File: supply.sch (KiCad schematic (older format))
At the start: 93 parts, among them IC12 74HC00PW, IC13 SN74LVC1G126DCKR, IC4 TPS7A0518PDBVT, J12 533980471, T3 BSS138APW, U1 LM3671MF-3.3/NOPB, U2 LM62440-Q1, U3 SN74LXC1T45DBVR, U5 LM3671MF-3.3/NOPB, U6 SIC477ED-T1-GE3

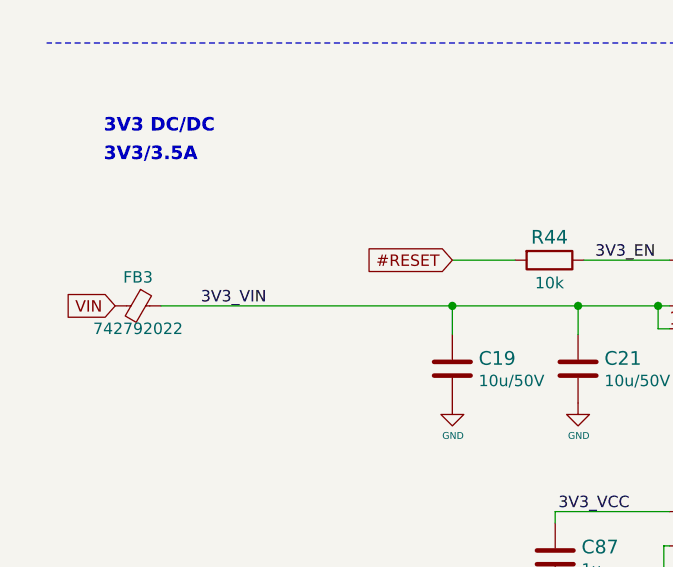
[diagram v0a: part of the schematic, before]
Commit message: Update MPS for FB2 FB3
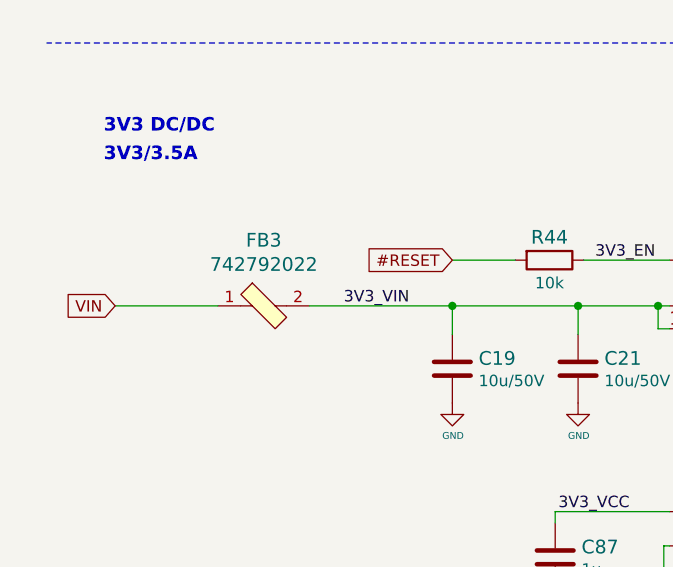
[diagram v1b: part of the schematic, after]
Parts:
- removed FB3: 742792022, jetson-nano-baseboard-footprints:0805-cap, symbol jetson-nano-baseboard:Ferrite_Bead_Small
- added FB3: 742792022, antmicro-footprints:0805-res, symbol antmicroFerriteBeadsandChips:742792022
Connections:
- net 3V3_VIN: now also FB3.2
- net VIN: now also FB3.1
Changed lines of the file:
@@
 Text Label 3050 5175 0    50   ~ 0
 3V3_EN
-$Comp
-L jetson-nano-baseboard:Ferrite_Bead_Small FB3
-U 1 1 61E2F9C4
-P 1050 5375
-F 0 "FB3" V 925 5375 50  0000 C CNN
-F 1 "742792022 " V 1150 5375 50  0000 C CNN
-F 2 "jetson-nano-baseboard-footprints:0805-cap" V 980 5375 50  0001 C CNN
-F 3 "~" H 1050 5375 50  0001 C CNN
-	1    1050 5375
-	0    1    1    0
-$EndComp
 Text GLabel 950  5375 0    50   Input ~ 0
 VIN
@@
 Text Label 3200 6275 2    50   ~ 0
 3V3_VCC
-Text Label 1325 5375 0    50   ~ 0
+Text Label 1950 5375 0    50   ~ 0
 3V3_VIN
 Text Label 4675 5750 0    50   ~ 0
@@
 	5775 4675 6225 4675
 Wire Wire Line
-	1150 5375 2425 5375
+	1800 5375 2425 5375
 Text Notes 15575 5400 0    59   ~ 12
 FAN 5V
@@
 Text GLabel 12350 6625 0    50   Input ~ 0
 1V8_SYS
+$Comp
+L antmicroFerriteBeadsandChips:742792022 FB3
+U 1 1 620C3704
+P 1600 5375
+F 0 "FB3" H 1600 5662 60  0000 C CNN
+F 1 "742792022" H 1600 5556 60  0000 C CNN
+F 2 "antmicro-footprints:0805-res" H 1800 5575 60  0001 L CNN
+F 3 "https://www.we-online.com/katalog/datasheet/742792022.pdf" H 1800 5675 60  0001 L CNN
+F 4 "742792022" H 1800 5875 60  0001 L CNN "MPN"
+F 5 "Wurth Electronic" H 1800 6475 60  0001 L CNN "Manufacturer"
+	1    1600 5375
+	1    0    0    -1
+$EndComp
+Wire Wire Line
+	1400 5375 950  5375
 $EndSCHEMATC

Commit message: Update libraries
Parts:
- FB3: footprint antmicro-footprints:0805-res -> jetson-nano-baseboard-footprints:0805-res; symbol antmicroFerriteBeadsandChips:742792022 -> jetson-nano-baseboard:742792022
- R76, R93: footprint antmicro-footprints:0402-res -> jetson-nano-baseboard-footprints:0402-res; symbol antmicroResistors0402:R_0R_0402 -> jetson-nano-baseboard:R_0R_0402
- U6: footprint antmicro-footprints:SIC47XED-T1-GE3 -> jetson-nano-baseboard-footprints:SIC47XED-T1-GE3; symbol antmicroDCDCConverters:SIC477ED-T1-GE3 -> jetson-nano-baseboard:SIC477ED-T1-GE3
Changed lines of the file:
@@
 	5625 1125 5700 1125
 $Comp
-L antmicroResistors0402:R_0R_0402 R93
+L jetson-nano-baseboard:R_0R_0402 R93
 U 1 1 625DF619
 P 5825 3050
 F 0 "R93" H 5825 3173 60  0000 C CNN
 F 1 "R_0R_0402" H 5825 2900 60  0001 C CNN
-F 2 "antmicro-footprints:0402-res" H 6025 3250 60  0001 L CNN
+F 2 "jetson-nano-baseboard-footprints:0402-res" H 6025 3250 60  0001 L CNN
 F 3 "" H 5825 3050 50  0001 C CNN
 F 4 "PANASONIC" H 6025 3450 60  0001 L CNN "Manufacturer"
@@
 VDD_5V_DCDC
 $Comp
-L antmicroResistors0402:R_0R_0402 R76
+L jetson-nano-baseboard:R_0R_0402 R76
 U 1 1 62667AA0
 P 3150 3025
 F 0 "R76" V 3195 2955 60  0000 R CNN
 F 1 "R_0R_0402" H 3150 2875 60  0001 C CNN
-F 2 "antmicro-footprints:0402-res" H 3350 3225 60  0001 L CNN
+F 2 "jetson-nano-baseboard-footprints:0402-res" H 3350 3225 60  0001 L CNN
 F 3 "" H 3150 3025 50  0001 C CNN
 F 4 "PANASONIC" H 3350 3425 60  0001 L CNN "Manufacturer"
@@
 Connection ~ 3150 3175
 $Comp
-L antmicroDCDCConverters:SIC477ED-T1-GE3 U6
+L jetson-nano-baseboard:SIC477ED-T1-GE3 U6
 U 1 1 628802FC
 P 4700 2575
 F 0 "U6" H 4700 3732 50  0000 C CNN
 F 1 "SIC477ED-T1-GE3" H 4700 3641 50  0000 C CNN
-F 2 "antmicro-footprints:SIC47XED-T1-GE3" H 4700 2575 50  0001 L BNN
+F 2 "jetson-nano-baseboard-footprints:SIC47XED-T1-GE3" H 4700 2575 50  0001 L BNN
 F 3 "https://www.vishay.com/docs/75786/sic47x.pdf" H 4700 2575 50  0001 L BNN
 F 4 "VISHAY" H 4700 2575 50  0001 L BNN "Manufacturer"
@@
 1V8_SYS
 $Comp
-L antmicroFerriteBeadsandChips:742792022 FB3
+L jetson-nano-baseboard:742792022 FB3
 U 1 1 620C3704
 P 1600 5375
 F 0 "FB3" H 1600 5662 60  0000 C CNN
 F 1 "742792022" H 1600 5556 60  0000 C CNN
-F 2 "antmicro-footprints:0805-res" H 1800 5575 60  0001 L CNN
+F 2 "jetson-nano-baseboard-footprints:0805-res" H 1800 5575 60  0001 L CNN
 F 3 "https://www.we-online.com/katalog/datasheet/742792022.pdf" H 1800 5675 60  0001 L CNN
 F 4 "742792022" H 1800 5875 60  0001 L CNN "MPN"
